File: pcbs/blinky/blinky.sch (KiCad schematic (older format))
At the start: 192 parts, among them J1 JACK IN, J3 CA1-9, J4 CB1-9, Q1 PMBT2222A,215, SW1 TACTILE, SW2 JS202011JCQN, U1 ATSAMD21E17, U2 MIC5225-3.3YM5, U3 TSOP36438TT, U4 IS31FL3731-SALS2

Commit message: ok, well that has been sent to china
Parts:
- removed H9: Lanyard Hole, MountingHole:MountingHole_2.5mm_Pad_Via, symbol Mechanical:MountingHole
- added H9: Lanyard, MountingHole:MountingHole_2.5mm_Pad_Via, symbol Mechanical:MountingHole_Pad
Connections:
- net GND: now also H9.1
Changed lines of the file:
@@
 $EndComp
 $Comp
-L Mechanical:MountingHole H9
-U 1 1 620E81F6
-P 1650 10550
-F 0 "H9" H 1750 10596 50  0000 L CNN
-F 1 "Lanyard Hole" H 1750 10505 50  0000 L CNN
-F 2 "MountingHole:MountingHole_2.5mm_Pad_Via" H 1650 10550 50  0001 C CNN
-F 3 "~" H 1650 10550 50  0001 C CNN
-	1    1650 10550
+L Mechanical:MountingHole_Pad H9
+U 1 1 62321B10
+P 1650 10400
+F 0 "H9" H 1750 10449 50  0000 L CNN
+F 1 "Lanyard" H 1750 10358 50  0000 L CNN
+F 2 "MountingHole:MountingHole_2.5mm_Pad_Via" H 1650 10400 50  0001 C CNN
+F 3 "~" H 1650 10400 50  0001 C CNN
+	1    1650 10400
 	1    0    0    -1
 $EndComp
+$Comp
+L power:GND #PWR0129
+U 1 1 62322FB2
+P 1650 10500
+F 0 "#PWR0129" H 1650 10250 50  0001 C CNN
+F 1 "GND" H 1655 10327 50  0000 C CNN
+F 2 "" H 1650 10500 50  0001 C CNN
+F 3 "" H 1650 10500 50  0001 C CNN
+	1    1650 10500
+	1    0    0    -1
+$EndComp

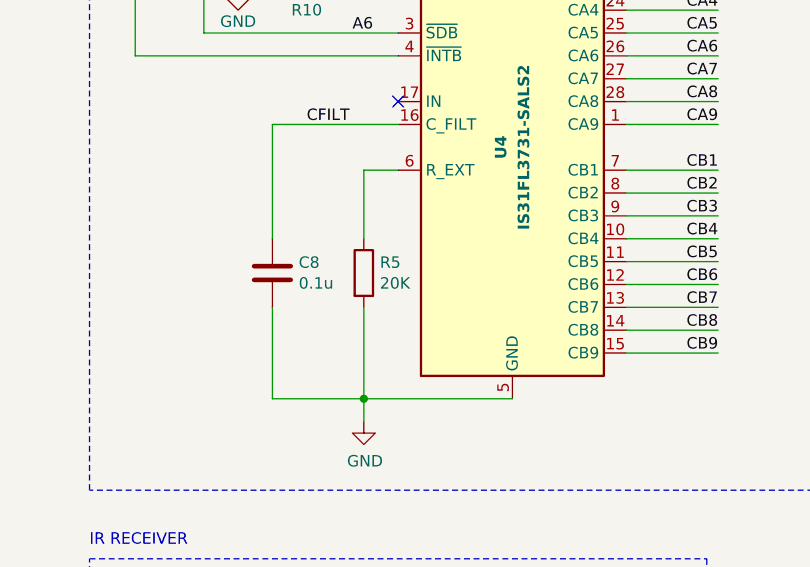
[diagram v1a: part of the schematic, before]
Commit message: Use 100K resistor for Rext to save power
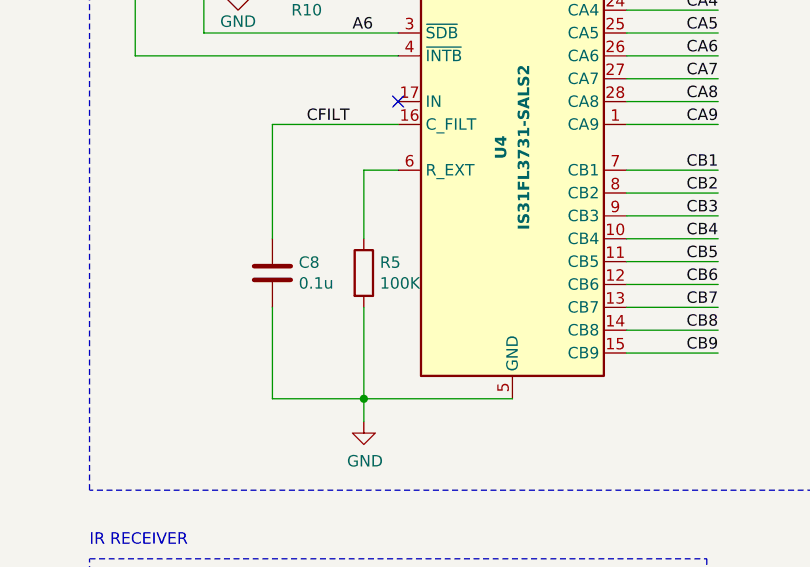
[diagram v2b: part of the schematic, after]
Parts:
- R5: value 20K -> 100K
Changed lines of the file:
@@
 P 12800 3500
 F 0 "R5" H 12870 3546 50  0000 L CNN
-F 1 "20K" H 12870 3455 50  0000 L CNN
+F 1 "100K" H 12870 3455 50  0000 L CNN
 F 2 "Resistor_SMD:R_0603_1608Metric" V 12730 3500 50  0001 C CNN
 F 3 "~" H 12800 3500 50  0001 C CNN
@@
 2RST
 $Comp
-L Joels_KiCad_Symbol_Library:TSOP36438TT U3
-U 1 1 629FCB03
-P 12450 5450
-F 0 "U3" H 12842 4885 50  0000 C CNN
-F 1 "TSOP36438TT" H 12842 4976 50  0000 C CNN
-F 2 "Joels KiCad Footprint Library:TSOP36438TT" H 13300 5550 50  0001 L CNN
-F 3 "https://www.mouser.com/datasheet/2/427/tsop362-464348.pdf" H 13300 5450 50  0001 L CNN
-F 4 "Infrared Receivers" H 13300 5350 50  0001 L CNN "Description"
-F 5 "5.3" H 13300 5250 50  0001 L CNN "Height"
-F 6 "Vishay" H 13300 5150 50  0001 L CNN "Manufacturer_Name"
-F 7 "TSOP36438TT" H 13300 5050 50  0001 L CNN "Manufacturer_Part_Number"
-F 8 "78-TSOP36438TT" H 13300 4950 50  0001 L CNN "Mouser Part Number"
-F 9 "https://www.mouser.co.uk/ProductDetail/Vishay-Semiconductors/TSOP36438TT?qs=b85dNVE93B5nGTLDDhv1%252Bg%3D%3D" H 13300 4850 50  0001 L CNN "Mouser Price/Stock"
-F 10 "TSOP36438TT" H 13300 4750 50  0001 L CNN "Arrow Part Number"
-F 11 "https://www.arrow.com/en/products/tsop36438tt/vishay?region=nac" H 13300 4650 50  0001 L CNN "Arrow Price/Stock"
-	1    12450 5450
-	-1   0    0    1
-$EndComp
-$Comp
 L Mechanical:MountingHole H1
 U 1 1 61EFA092
@@
 	1    0    0    -1
 $EndComp
+$Comp
+L Joels_KiCad_Symbol_Library:TSOP36438TT U3
+U 1 1 629FCB03
+P 12450 5450
+F 0 "U3" H 12842 4885 50  0000 C CNN
+F 1 "TSOP36438TT" H 12842 4976 50  0000 C CNN
+F 2 "Joels KiCad Footprint Library:TSOP36438TT" H 13300 5550 50  0001 L CNN
+F 3 "https://www.mouser.com/datasheet/2/427/tsop362-464348.pdf" H 13300 5450 50  0001 L CNN
+F 4 "Infrared Receivers" H 13300 5350 50  0001 L CNN "Description"
+F 5 "5.3" H 13300 5250 50  0001 L CNN "Height"
+F 6 "Vishay" H 13300 5150 50  0001 L CNN "Manufacturer_Name"
+F 7 "TSOP36438TT" H 13300 5050 50  0001 L CNN "Manufacturer_Part_Number"
+F 8 "78-TSOP36438TT" H 13300 4950 50  0001 L CNN "Mouser Part Number"
+F 9 "https://www.mouser.co.uk/ProductDetail/Vishay-Semiconductors/TSOP36438TT?qs=b85dNVE93B5nGTLDDhv1%252Bg%3D%3D" H 13300 4850 50  0001 L CNN "Mouser Price/Stock"
+F 10 "TSOP36438TT" H 13300 4750 50  0001 L CNN "Arrow Part Number"
+F 11 "https://www.arrow.com/en/products/tsop36438tt/vishay?region=nac" H 13300 4650 50  0001 L CNN "Arrow Price/Stock"
+	1    12450 5450
+	-1   0    0    1
+$EndComp
 $EndSCHEMATC

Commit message: Updated schematics and PCB to fix all known bugs
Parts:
- removed BT2: CR2032, Joels KiCad Footprint Library:BatteryHolder_Keystone_3034_Minimum_Pad, symbol Device:Battery_Cell
- removed J1: JACK IN, Joels KiCad Footprint Library:SOIC_clipProgSmall, symbol Connector_Generic:Conn_02x04_Counter_Clockwise
- removed U1: ATSAMD21E17, Joels KiCad Footprint Library:ATSAMD21E17_32Pin_TQFP, symbol Joels_KiCad_Symbol_Library:ATSAMD21E18A-AF
- added BT2, BT4: CR2032 (-) PAD, Joels KiCad Footprint Library:Keystone_2992_Negative_Contact_Pad, symbol Joels_KiCad_Symbol_Library:Battery_Negative_Pad
- added BT3: CR2032 (+) CLIP, Joels KiCad Footprint Library:BatteryHolder_Keystone_3034_Pos_Clip, symbol Joels_KiCad_Symbol_Library:Battery_Positive_Clip
- added J2: TC2050-IDC, Joels KiCad Footprint Library:TAG-CONNECT_TC2050-IDC, symbol Joels_KiCad_Symbol_Library:TC2050-IDC
- added U1: ATSAMD21E17L-AF, Joels KiCad Footprint Library:ATSAMD21E17_32Pin_TQFP, symbol Joels_KiCad_Symbol_Library:ATSAMD21E17L-AF
- BT1: value CR2032 -> CR2032 (+) CLIP; footprint Joels KiCad Footprint Library:BatteryHolder_Keystone_3034_Minimum_Pad -> Joels KiCad Footprint Library:BatteryHolder_Keystone_3034_Pos_Clip; symbol Device:Battery_Cell -> Joels_KiCad_Symbol_Library:Battery_Positive_Clip
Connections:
- net +3V3: now also J2.2, U1.28 (VDDIN), U1.9 (VDDANA)
- net +5V: now also J2.8
- net 2RST: now also U1.25 (~RESET)
- net A0: now also U1.1 (PA02)
- net A1: now also U1.2 (PA03)
- net A2: now also U1.5 (PA04)
- net A3: now also U1.6 (PA05)
- net A6: now also U1.7 (PA06)
- net A7: now also J2.3, U1.8 (PA07)
- net GND: now also BT4.1 (Pin_1), J2.5, U1.10 (GND), U1.26 (GNDA)
- net SCL: now also U1.18 (PA17)
- net SDA: now also U1.17 (PA16)
- net SWCLK: now also J2.9, U1.29 (PA30/SWCLK)
- net SWDIO: now also J2.10, U1.30 (PA31/SWDIO)
- net VDDCORE: now also U1.27 (VDDCORE)
- net ~RESET: now also J2.6
- new net: BT2.1 (Pin_1), BT3.1 (Pin_1)
- no-connect marks 22 -> 24
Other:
- note added: "MCU - SAMD21E17L"
- note added: "POWER SWITCH"
- note added: "SAMD21ExxL VARIANT HAS DIFFERENT PINOUT THAN OTHER SAMD21E CHIPS"
- note added: "TAG-CONNECT FLASH AND TEST"
- note added: "TWO CR2032 BATTERIES\nWITH SEPARATE (+) CLIP\nAND (-) CONTACT PAD"
- note removed: "CONTROL"
- note removed: "MCU - ATSAMD21E17"
- note removed: "SOIC-8 CLIP FLASH AND TEST"
- moved on the sheet: C1, C5, C6, SW1, SW2, U2
